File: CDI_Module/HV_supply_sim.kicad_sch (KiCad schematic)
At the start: 0 parts

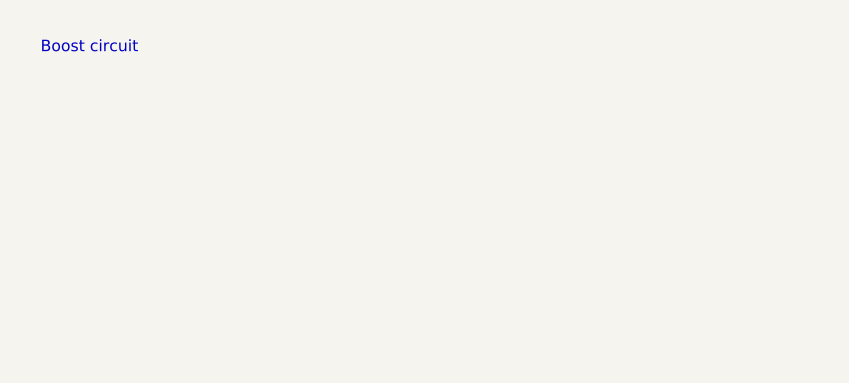
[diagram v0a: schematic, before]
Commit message: Updated to Kicad 8.0
Also added Highvoltage circuit
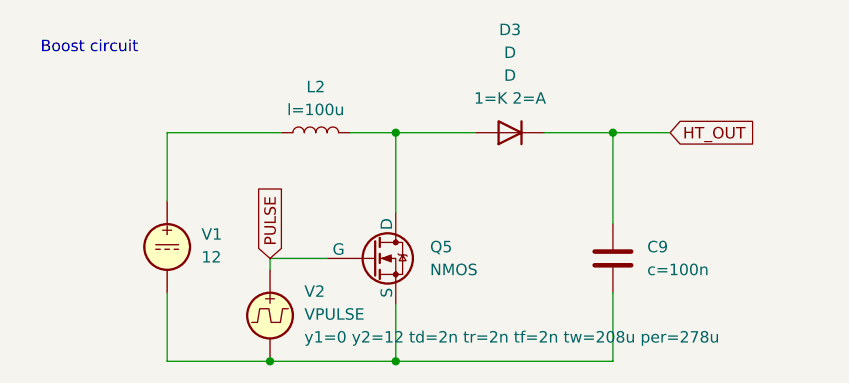
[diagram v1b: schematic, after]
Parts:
- added C9: ${SIM.PARAMS}, symbol Device:C
- added D3: D, symbol Simulation_SPICE:D
- added L2: ${SIM.PARAMS}, symbol Device:L
- added Q5: NMOS, symbol Simulation_SPICE:NMOS
- added V1: 12, symbol Simulation_SPICE:VDC
- added V2: VPULSE, symbol Simulation_SPICE:VPULSE
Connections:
- new net: C9.2, Q5.3 (S), V1.2, V2.2
- new net: L2.1, V1.1
- new net: D3.2 (A), L2.2, Q5.1 (D)
- new net HT_OUT: C9.1, D3.1 (K)
- new net PULSE: Q5.2 (G), V2.1
